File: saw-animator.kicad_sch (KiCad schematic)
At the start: 63 parts, among them J1 Conn_02x05_Odd_Even, J10 AudioJack2_SwitchT, J2 Conn_01x03_Socket, J3 Conn_01x03_Socket, J4 Conn_01x03_Socket, J5 Conn_01x03_Pin, J6 Conn_01x03_Pin, J7 Conn_01x03_Pin, J8 AudioJack2_SwitchT, J9 AudioJack2_SwitchT, Q1 BC547, U1 TL074, U2 TL074

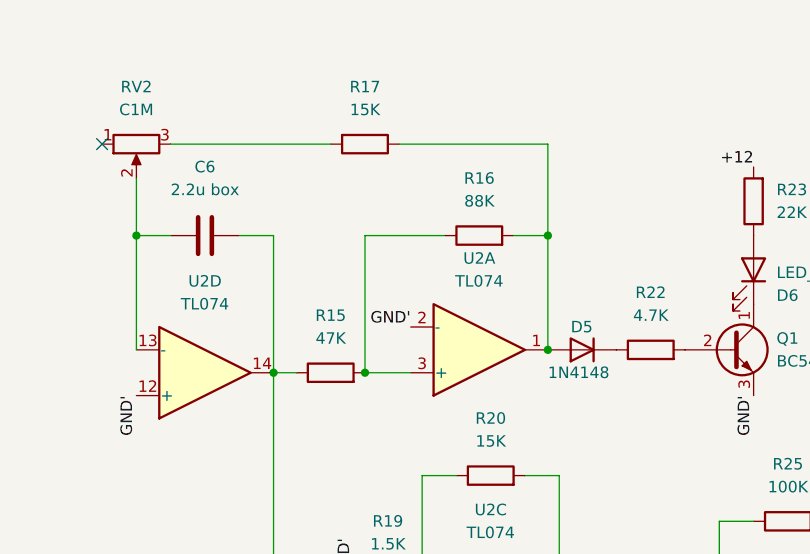
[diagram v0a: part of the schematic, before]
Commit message: fix: updating resistances to easily obtainable values
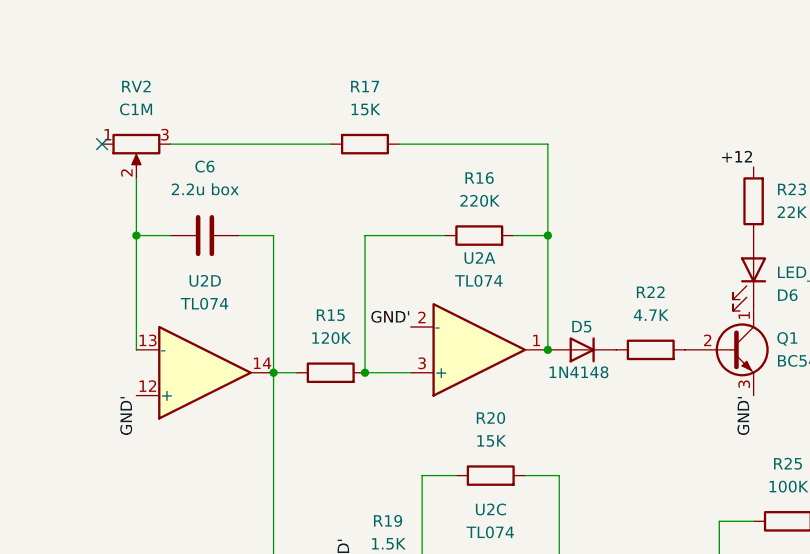
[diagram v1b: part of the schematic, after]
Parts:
- R15: value 47K -> 120K
- R16: value 88K -> 220K
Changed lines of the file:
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@@
       (effects (font (size 1.27 1.27)))
     )
-    (property "Value" "47K" (at 80.01 49.53 90)
+    (property "Value" "120K" (at 80.01 49.53 90)
       (effects (font (size 1.27 1.27)))
     )
@@
       (effects (font (size 1.27 1.27)))
     )
-    (property "Value" "88K" (at 96.52 34.29 90)
-      (effects (font (size 1.27 1.27)))
-    )
+    (property "Value" "220K" (at 96.52 34.29 90)
+      (effects (font (size 1.27 1.27)))
+    )
